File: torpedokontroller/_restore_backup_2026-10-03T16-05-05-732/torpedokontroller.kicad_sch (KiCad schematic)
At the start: 0 parts

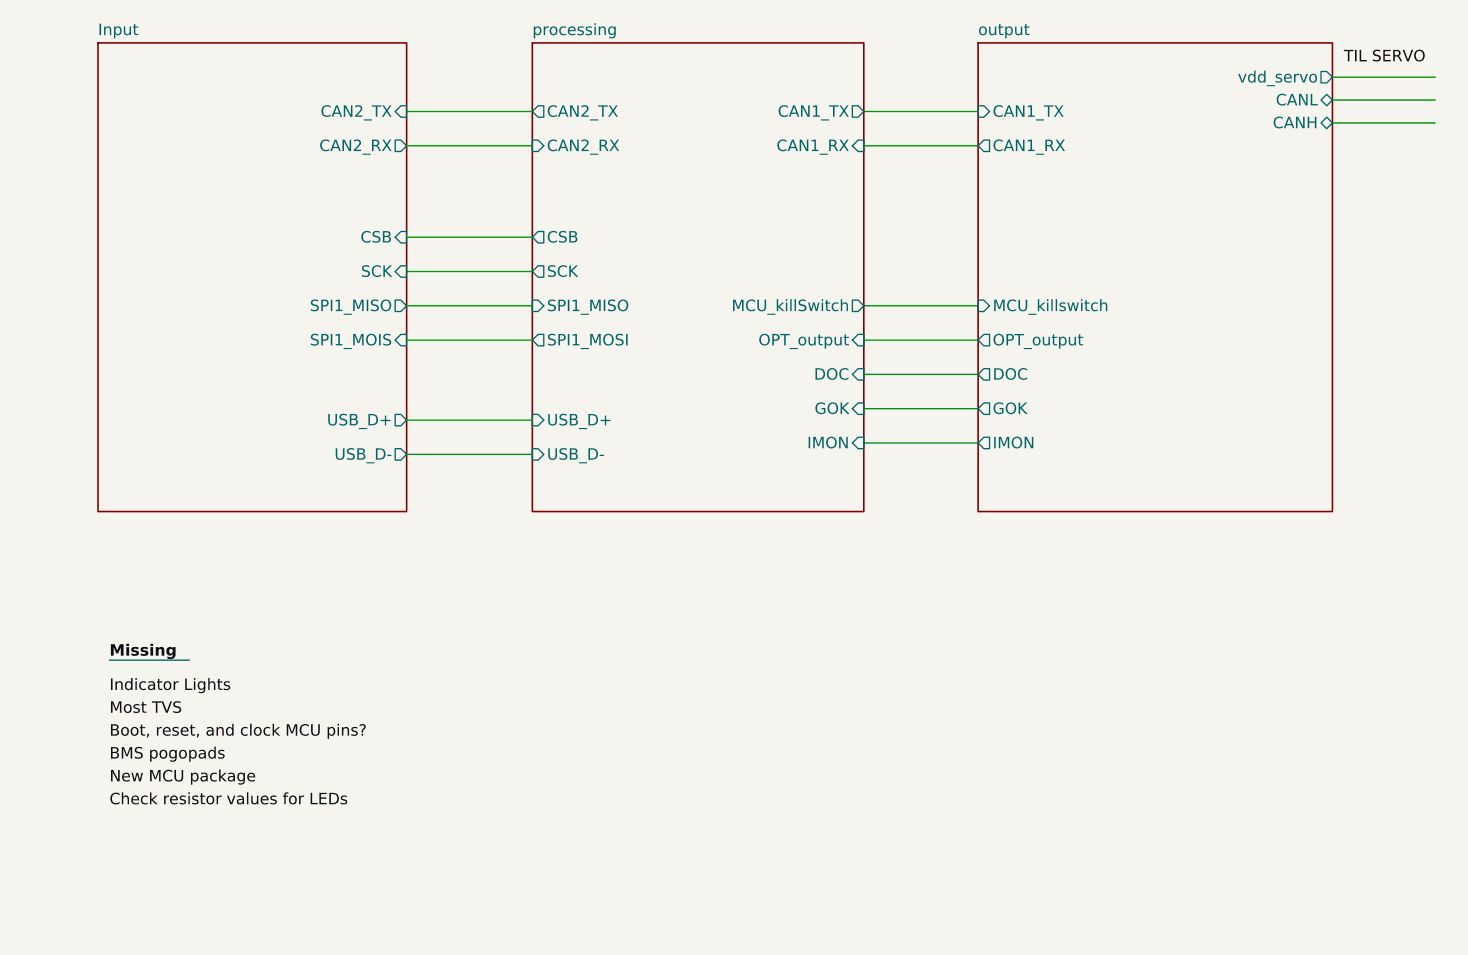
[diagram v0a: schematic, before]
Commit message: v0.5
USB2.0 implemented fr
many other things
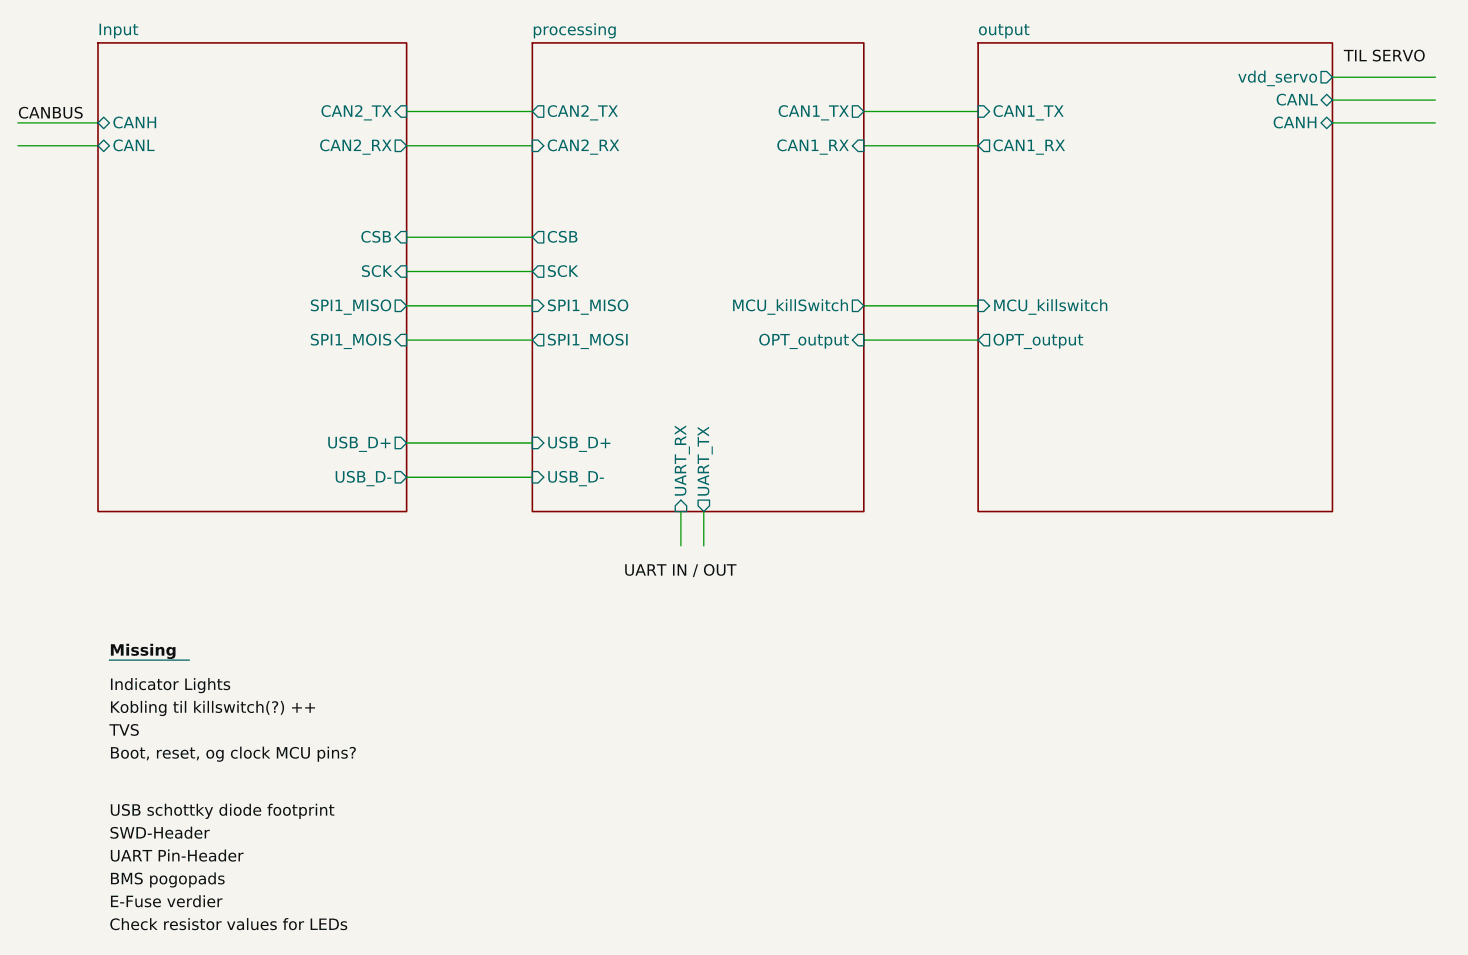
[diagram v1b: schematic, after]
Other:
- sheet Input ports: added CANH, CANL; removed none
- sheet output ports: added none; removed DOC, GOK, IMON
- sheet processing ports: added UART_RX, UART_TX; removed DOC, GOK, IMON
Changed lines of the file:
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@@
 	(paper "A5")
 	(title_block
-		(date "2026-10-03")
+		(date "2026-10-02")
 		(comment 1 "Simon Torvund")
 	)
@@
 	(wire
 		(pts
-			(xy 116.84 74.93) (xy 129.54 74.93)
-		)
-		(stroke
-			(width 0)
-			(type default)
-		)
-	)
-	(wire
-		(pts
 			(xy 168.91 34.29) (xy 180.34 34.29)
 		)
@@
 	(wire
 		(pts
+			(xy 96.52 82.55) (xy 96.52 86.36)
+		)
+		(stroke
+			(width 0)
+			(type default)
+		)
+	)
+	(wire
+		(pts
 			(xy 116.84 38.1) (xy 129.54 38.1)
 		)
@@
 	(wire
 		(pts
+			(xy 22.86 39.37) (xy 31.75 39.37)
+		)
+		(stroke
+			(width 0)
+			(type default)
+		)
+	)
+	(wire
+		(pts
 			(xy 116.84 41.91) (xy 129.54 41.91)
 		)
@@
 	(wire
 		(pts
-			(xy 116.84 71.12) (xy 129.54 71.12)
-		)
-		(stroke
-			(width 0)
-			(type default)
-		)
-	)
-	(wire
-		(pts
-			(xy 66.04 76.2) (xy 80.01 76.2)
+			(xy 66.04 78.74) (xy 80.01 78.74)
 		)
 		(stroke
@@
 	(wire
 		(pts
-			(xy 66.04 72.39) (xy 80.01 72.39)
+			(xy 66.04 74.93) (xy 80.01 74.93)
 		)
 		(stroke
@@
 	(wire
 		(pts
-			(xy 116.84 67.31) (xy 129.54 67.31)
+			(xy 22.86 41.91) (xy 31.75 41.91)
+		)
+		(stroke
+			(width 0)
+			(type default)
+		)
+	)
+	(wire
+		(pts
+			(xy 99.06 82.55) (xy 99.06 86.36)
 		)
 		(stroke
@@
 	)
 	(label "Check resistor values for LEDs"
-		(at 33.02 115.57 0)
+		(at 33.02 129.54 0)
+		(effects
+			(font
+				(size 1.27 1.27)
+			)
+			(justify left bottom)
+		)
+	)
+	(label "SWD-Header"
+		(at 33.02 119.38 0)
+		(effects
+			(font
+				(size 1.27 1.27)
+			)
+			(justify left bottom)
+		)
+	)
+	(label "CANBUS"
+		(at 22.86 39.37 0)
+		(effects
+			(font
+				(size 1.27 1.27)
+			)
+			(justify left bottom)
+		)
+	)
+	(label "Kobling til killswitch(?) ++"
+		(at 33.02 105.41 0)
 		(effects
 			(font
@@
 		)
 	)
-	(label "New MCU package"
-		(at 33.02 113.03 0)
+	(label "E-Fuse verdier"
+		(at 33.02 127 0)
+		(effects
+			(font
+				(size 1.27 1.27)
+			)
+			(justify left bottom)
+		)
+	)
+	(label "UART Pin-Header"
+		(at 33.02 121.92 0)
 		(effects
 			(font
@@
 	)
 	(label "BMS pogopads"
-		(at 33.02 110.49 0)
-		(effects
-			(font
-				(size 1.27 1.27)
-			)
-			(justify left bottom)
-		)
-	)
-	(label "Most TVS"
-		(at 33.02 105.41 0)
+		(at 33.02 124.46 0)
+		(effects
+			(font
+				(size 1.27 1.27)
+			)
+			(justify left bottom)
+		)
+	)
+	(label "TVS"
+		(at 33.02 107.95 0)
+		(effects
+			(font
+				(size 1.27 1.27)
+			)
+			(justify left bottom)
+		)
+	)
+	(label "USB schottky diode footprint"
+		(at 33.02 116.84 0)
 		(effects
 			(font
@@
 		)
 	)
-	(label "Boot, reset, and clock MCU pins?"
-		(at 33.02 107.95 0)
+	(label "UART IN {slash} OUT"
+		(at 90.17 90.17 0)
+		(effects
+			(font
+				(size 1.27 1.27)
+			)
+			(justify left bottom)
+		)
+	)
+	(label "Boot, reset, og clock MCU pins?"
+		(at 33.02 110.49 0)
 		(effects
 			(font
@@
 			)
 		)
+		(pin "UART_RX" input
+			(at 96.52 82.55 270)
+			(effects
+				(font
+					(size 1.27 1.27)
+				)
+				(justify left)
+			)
+		)
+		(pin "UART_TX" output
+			(at 99.06 82.55 270)
+			(effects
+				(font
+					(size 1.27 1.27)
+				)
+				(justify left)
+			)
+		)
 		(pin "USB_D+" input
-			(at 80.01 72.39 180)
+			(at 80.01 74.93 180)
 			(effects
 				(font
@@
 		)
 		(pin "USB_D-" input
-			(at 80.01 76.2 180)
-			(effects
-				(font
-					(size 1.27 1.27)
-				)
-				(justify left)
-			)
-		)
-		(pin "DOC" input
-			(at 116.84 67.31 0)
-			(effects
-				(font
-					(size 1.27 1.27)
-				)
-				(justify right)
-			)
-		)
-		(pin "GOK" input
-			(at 116.84 71.12 0)
-			(effects
-				(font
-					(size 1.27 1.27)
-				)
-				(justify right)
-			)
-		)
-		(pin "IMON" input
-			(at 116.84 74.93 0)
-			(effects
-				(font
-					(size 1.27 1.27)
-				)
-				(justify right)
+			(at 80.01 78.74 180)
+			(effects
+				(font
+					(size 1.27 1.27)
+				)
+				(justify left)
 			)
 		)
@@
 			)
 		)
-		(pin "DOC" output
-			(at 129.54 67.31 180)
-			(effects
-				(font
-					(size 1.27 1.27)
-				)
-				(justify left)
-			)
-		)
-		(pin "GOK" output
-			(at 129.54 71.12 180)
-			(effects
-				(font
-					(size 1.27 1.27)
-				)
-				(justify left)
-			)
-		)
-		(pin "IMON" output
-			(at 129.54 74.93 180)
-			(effects
-				(font
-					(size 1.27 1.27)
-				)
-				(justify left)
-			)
-		)
 		(instances
 			(project "torpedokontroller"
@@
 		)
 		(pin "USB_D+" output
-			(at 66.04 72.39 0)
+			(at 66.04 74.93 0)
 			(effects
 				(font
@@
 		)
 		(pin "USB_D-" output
-			(at 66.04 76.2 0)
+			(at 66.04 78.74 0)
 			(effects
 				(font
@@
 			)
 		)
+		(pin "CANH" bidirectional
+			(at 31.75 39.37 180)
+			(effects
+				(font
+					(size 1.27 1.27)
+				)
+				(justify left)
+			)
+		)
+		(pin "CANL" bidirectional
+			(at 31.75 41.91 180)
+			(effects
+				(font
+					(size 1.27 1.27)
+				)
+				(justify left)
+			)
+		)
